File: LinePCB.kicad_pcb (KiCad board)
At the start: 2 copper layers, 174.9 x 165 mm, 205 parts, among them J1 Conn_01x12, U1 MCP3008, U2 MCP3008, U3 MCP3008, U4 MCP3008, U5 MCP3008, U6 MCP3008

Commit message: a
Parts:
- moved D68 219.6 mm to (231.0, 51.5)
- moved D13 212.5 mm to (211.8, 30.2)
- moved D71 212.2 mm to (231.0, 60.6)
- moved D34 207.5 mm to (216.6, 57.5)
- moved D44 200.4 mm to (221.4, 51.5)
- moved D7 200.0 mm to (207.0, 48.4)
- moved D12 198.7 mm to (207.0, 63.6)
- moved D75 196.9 mm to (235.8, 36.3)
- moved D33 193.9 mm to (216.6, 54.5)
- moved D15 190.2 mm to (211.8, 36.3)
- moved D5 187.8 mm to (207.0, 42.3)
- moved D47 185.6 mm to (221.4, 60.6)
- moved D10 185.2 mm to (207.0, 57.5)
- moved D4 181.8 mm to (207.0, 39.3)
- moved D3 179.4 mm to (207.0, 36.3)
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
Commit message: Placement Finished
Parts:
- moved R29 252.7 mm to (14.9, 115.2), turned to 10.1506 degrees
- moved R14 249.8 mm to (17.2, 120.4), turned to 89.8972 degrees
- moved R27 248.3 mm to (22.8, 118.3), turned to 79.0726 degrees
- moved R32 248.2 mm to (13.6, 103.1), turned to 2.0301 degrees
- moved R28 247.7 mm to (14.0, 90.8), turned to -6.09035 degrees
- moved R31 240.6 mm to (17.2, 79.6), turned to -89.8972 degrees
- moved R15 240.3 mm to (27.0, 122.5), turned to 35 degrees
- moved R60 239.6 mm to (55.5, 168.2), turned to -39.7842 degrees
- moved R62 237.8 mm to (44.6, 147.6), turned to 35 degrees
- moved R16 236.6 mm to (34.1, 132.5), turned to 35 degrees
- moved R13 235.4 mm to (14.0, 109.2), turned to 6.09035 degrees
- moved R64 235.2 mm to (58.2, 175.7), turned to 59.8914 degrees
- moved R12 234.3 mm to (13.6, 96.9), turned to -2.0301 degrees
- moved R63 234.2 mm to (51.6, 157.6), turned to 35 degrees
- moved R33 233.8 mm to (41.1, 142.6), turned to 35 degrees
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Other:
- board size 174.9 x 165 mm -> 178 x 169.8 mm

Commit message: Placement
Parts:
- added D97: LED, LED_SMD:LED_0805_2012Metric_Pad1.15x1.40mm_HandSolder, F.Cu at (-6.51, 116.5)
- added J3: Conn_01x03, Connector_JST:JST_XH_B3B-XH-A_1x03_P2.50mm_Vertical, F.Cu at (-4.16, 130.4)
- added R103: 25, Package_TO_SOT_THT:TO-220-2_Vertical, F.Cu at (-16.5, 95.8)
- added U10: Optocoupler, Package_DIP:DIP-4_W7.62mm, F.Cu at (-18.1, 117.1)
- added U11: 210, Resistor_SMD:R_0805_2012Metric_Pad1.20x1.40mm_HandSolder, F.Cu at (-5.79, 99.3)
- added U12: 2200, Capacitor_THT:CP_Radial_D18.0mm_P7.50mm, F.Cu at (29.3, 109.4)
- added U13: 2200, Capacitor_THT:CP_Radial_D18.0mm_P7.50mm, F.Cu at (31.3, 89.2)
- added U14: 210, Resistor_SMD:R_0805_2012Metric_Pad1.20x1.40mm_HandSolder, F.Cu at (-5.79, 102.2)
- added U15: Oprocoupler, Package_DIP:DIP-4_W7.62mm, F.Cu at (-18.1, 123.7)
- added U16: 10k, Resistor_SMD:R_0805_2012Metric_Pad1.20x1.40mm_HandSolder, F.Cu at (-5.79, 105.2)
- added U17: N channel, Package_TO_SOT_THT:TO-220-3_Vertical, F.Cu at (-16.5, 107.8)
- added U18: D, Diode_THT:D_5W_P12.70mm_Horizontal, F.Cu at (52.3, 106.3)
- added U19: 10K, Resistor_SMD:R_0805_2012Metric_Pad1.20x1.40mm_HandSolder, F.Cu at (-5.79, 108.2)
- added U20: Conn_01x02, SMDPads:Pads, B.Cu at (42.0, 99.7)
- added U7: 30k, Resistor_SMD:R_0805_2012Metric_Pad1.20x1.40mm_HandSolder, F.Cu at (-5.79, 93.4)
- added U8: 115k, Resistor_SMD:R_0805_2012Metric_Pad1.20x1.40mm_HandSolder, F.Cu at (-5.79, 96.3)
- added U9: BSP89, Package_TO_SOT_THT:TO-220-3_Vertical, F.Cu at (-16.5, 101.8)
- D1, D10, D11, D12, D13, D14, D15, D16, D17, D18, D19, D2, D20, D21, D22, D23, D24, D25, D26, D27, D28, D29, D3, D30, D31, D32, D33, D34, D35, D36, D37, D38, D39, D4, D40, D41, D42, D43, D44, D45, D46, D47, D48, D49, D5, D50, D51, D52, D53, D54, D55, D56, D57, D58, D59, D6, D60, D61, D62, D63, D64, D65, D66, D67, D68, D69, D7, D70, D71, D72, D73, D74, D75, D76, D77, D78, D79, D8, D80, D81, D82, D83, D84, D85, D86, D87, D88, D89, D9, D90, D91, D92, D93, D94, D95, D96, R1, R10, R100, R101, R102, R11, R12, R13, R14, R15, R16, R17, R18, R19, R2, R20, R21, R22, R23, R24, R25, R26, R27, R28, R29, R3, R30, R31, R32, R33, R34, R35, R36, R37, R38, R39, R4, R40, R41, R42, R43, R44, R45, R46, R47, R48, R49, R5, R50, R51, R52, R53, R54, R55, R56, R57, R58, R59, R6, R60, R61, R62, R63, R64, R65, R66, R67, R68, R69, R7, R70, R71, R72, R73, R74, R75, R76, R77, R78, R79, R8, R80, R81, R82, R83, R84, R85, R86, R87, R88, R89, R9, R90, R91, R92, R93, R94, R95, R96, R97, R98, R99, U1, U2, U3, U4, U5, U6: moved to B.Cu
- moved U4 188.7 mm to (94.6, 152.0), turned to 180 degrees
- moved U3 174.8 mm to (106.4, 151.9), turned to 180 degrees
- moved D85 173.1 mm to (13.4, 98.5), turned to -0.97863 degrees
- moved R90 173.1 mm to (13.4, 101.6), turned to 1.05149 degrees
- moved R69 172.9 mm to (13.5, 95.5), turned to -3.00875 degrees
- moved D74 172.9 mm to (13.5, 104.7), turned to -176.918 degrees
- moved D17 172.9 mm to (186.4, 100.0), turned to 0 degrees
- moved R12 172.8 mm to (186.3, 96.9), turned to -177.97 degrees
- moved R32 172.8 mm to (186.3, 103.1), turned to 177.97 degrees
- moved D70 172.5 mm to (13.7, 92.4), turned to 174.961 degrees
- moved R68 172.4 mm to (13.7, 107.7), turned to 5.11172 degrees
- moved D28 172.4 mm to (186.2, 93.9), turned to -175.94 degrees
- moved D29 172.4 mm to (186.2, 106.1), turned to 175.94 degrees
- moved R13 171.9 mm to (185.9, 109.2), turned to 173.91 degrees
- moved R28 171.9 mm to (185.9, 90.8), turned to -173.91 degrees
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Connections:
- J1 pad 9: 5V -> Kicker
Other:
- outline, holes or cut-outs redrawn

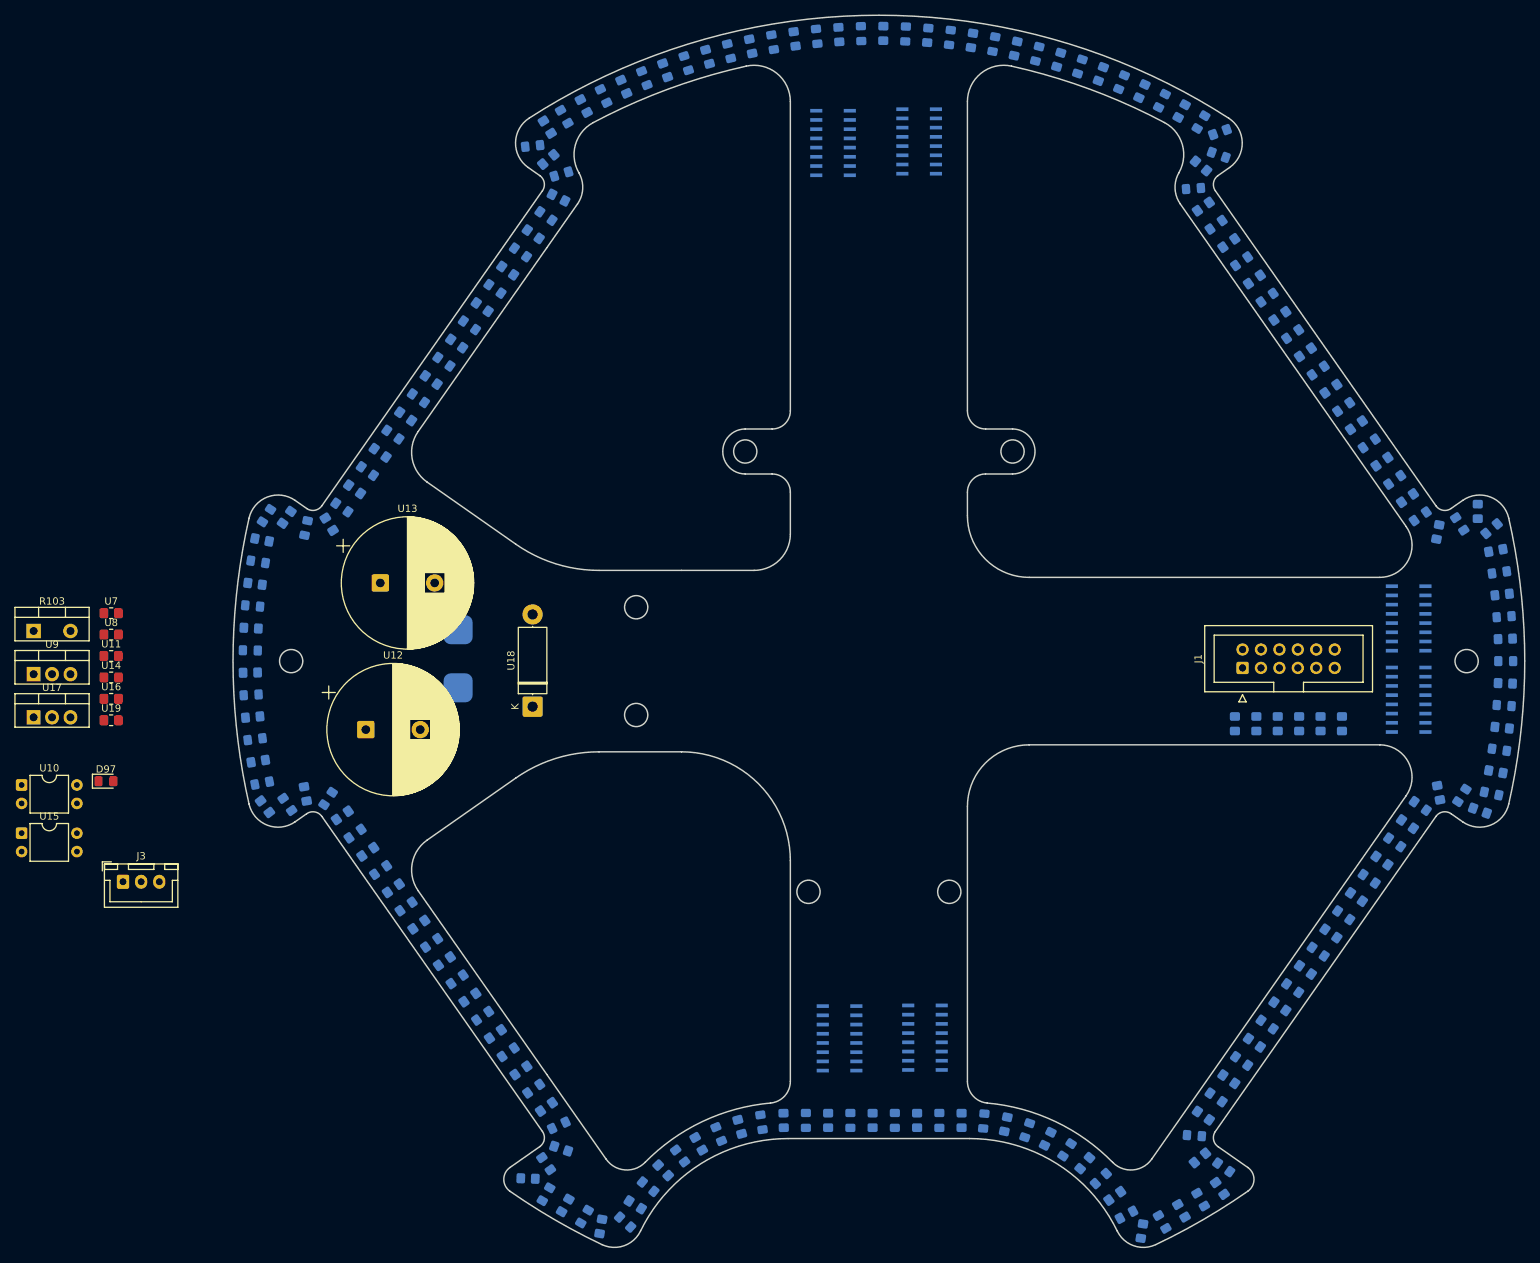
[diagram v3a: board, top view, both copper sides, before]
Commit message: Finished routing, needs clearing up clearance errors
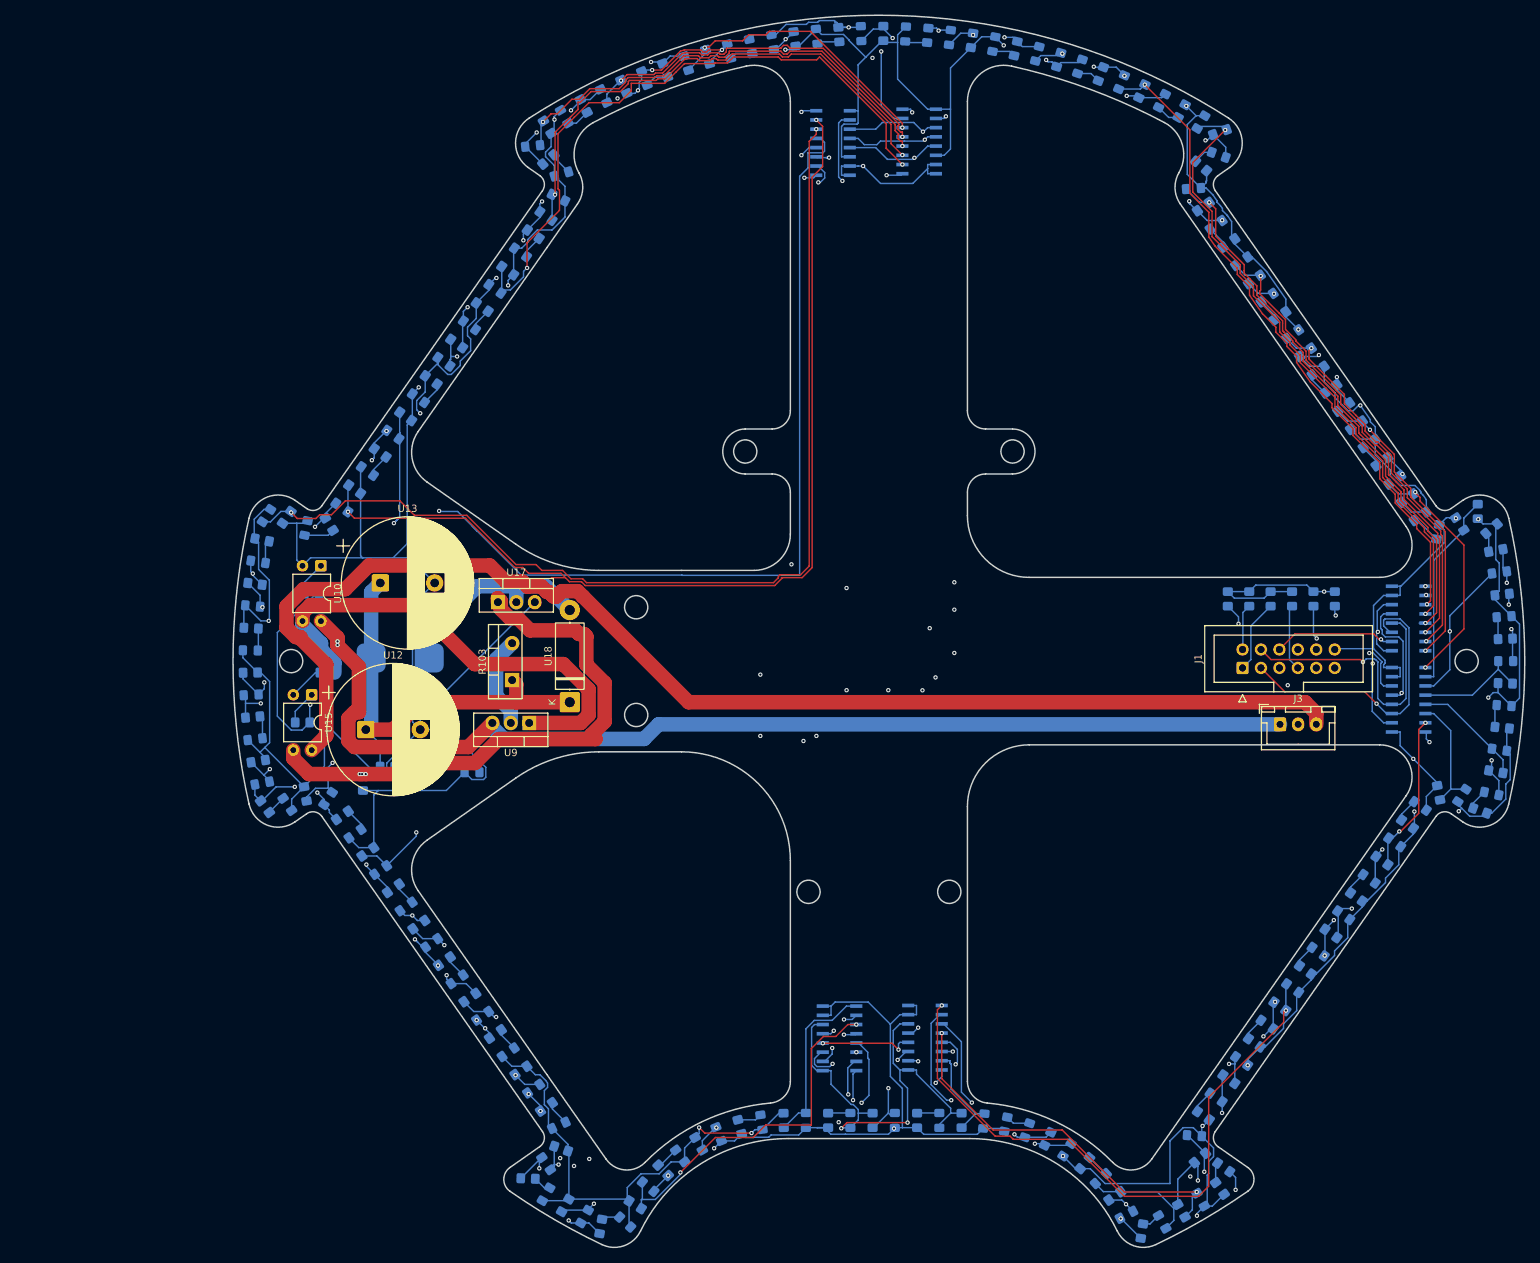
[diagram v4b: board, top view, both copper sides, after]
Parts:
- D97, U11, U14, U16, U19, U7, U8: moved to B.Cu
- moved J3 160.9 mm to (155.3, 108.7)
- moved U9 68.6 mm to (51.8, 108.5), turned to 180 degrees
- moved R103 66.3 mm to (49.5, 102.6), turned to 90 degrees
- moved U17 65.9 mm to (47.5, 91.9)
- moved U10 51.1 mm to (23.1, 86.9), turned to -90 degrees
- moved D97 50.5 mm to (43.9, 115.3)
- moved U15 44.3 mm to (21.8, 104.6), turned to -90 degrees
- moved U16 39.2 mm to (32.3, 114.6), turned to 180 degrees
- moved U19 35.8 mm to (28.9, 116.8), turned to 90 degrees
- moved U8 30.2 mm to (24.0, 101.6)
- moved U7 30.2 mm to (24.1, 97.5)
- moved U11 28.9 mm to (21.8, 90.7)
- moved U14 27.1 mm to (20.6, 108.5), turned to 180 degrees
- moved R97 23.3 mm to (148.1, 91.4), turned to -90 degrees
- moved R102 22.0 mm to (162.8, 91.4), turned to -90 degrees
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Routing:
- net GND: track 0.00 -> 1086.6 mm, vias 0 -> 39
- net 3.3V: track 0.00 -> 938.8 mm, vias 0 -> 47
- net MOSI: track 0.00 -> 245.8 mm, vias 0 -> 6
- net SCK1: track 0.00 -> 241.8 mm, vias 0 -> 7
- net MISO: track 0.00 -> 241.2 mm, vias 0 -> 5
- net 12V: track 0.00 -> 178.1 mm
- net Kicker: track 0.00 -> 169.7 mm, vias 0 -> 1
- net Ch35: track 0.00 -> 166.0 mm, vias 0 -> 3
- net Ch34: track 0.00 -> 156.2 mm, vias 0 -> 3
- net Ch36: track 0.00 -> 152.6 mm, vias 0 -> 3
- net 48V: track 0.00 -> 152.2 mm, vias 0 -> 2
- net Ch37: track 0.00 -> 152.0 mm, vias 0 -> 2
- net Ch33: track 0.00 -> 150.8 mm, vias 0 -> 4
- net Ch40: track 0.00 -> 145.9 mm, vias 0 -> 3
- net Ch38: track 0.00 -> 143.6 mm, vias 0 -> 2
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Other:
- copper layers 2 -> 4

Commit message: Done
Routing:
- net 3.3V: track 938.8 -> 966.5 mm, vias 47 -> 53
- net GND: track 1086.6 -> 1082.6 mm
- net Ch29: track 62.5 -> 66.2 mm
- net Ch41: track 106.5 -> 109.8 mm
- net Ch32: track 92.9 -> 95.5 mm
- net Ch40: track 145.9 -> 143.6 mm
- net Ch39: track 137.7 -> 135.6 mm
- net Ch42: track 90.2 -> 88.5 mm
- net Ch31: track 79.9 -> 81.3 mm
- net Ch27: track 49.6 -> 50.9 mm, vias 2 -> 3
- net Ch35: track 166.0 -> 164.7 mm
- net Ch19: track 55.0 -> 56.1 mm
- net Ch37: track 152.0 -> 151.0 mm
- net Ch18: track 73.6 -> 74.4 mm
- net Ch28: track 58.5 -> 59.2 mm
- added copper zone on B.Cu, net GND
- added copper zone on F.Cu, net GND
- added copper zone on In1.Cu, net GND
- added copper zone on In2.Cu, net GND
